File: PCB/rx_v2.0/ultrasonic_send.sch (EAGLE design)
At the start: 30 parts, among them J1 SBWD, J2 UART, J3 AD, J4 function, J5 pwr_5V, J6 AD, Q3 AMS1117-3.3

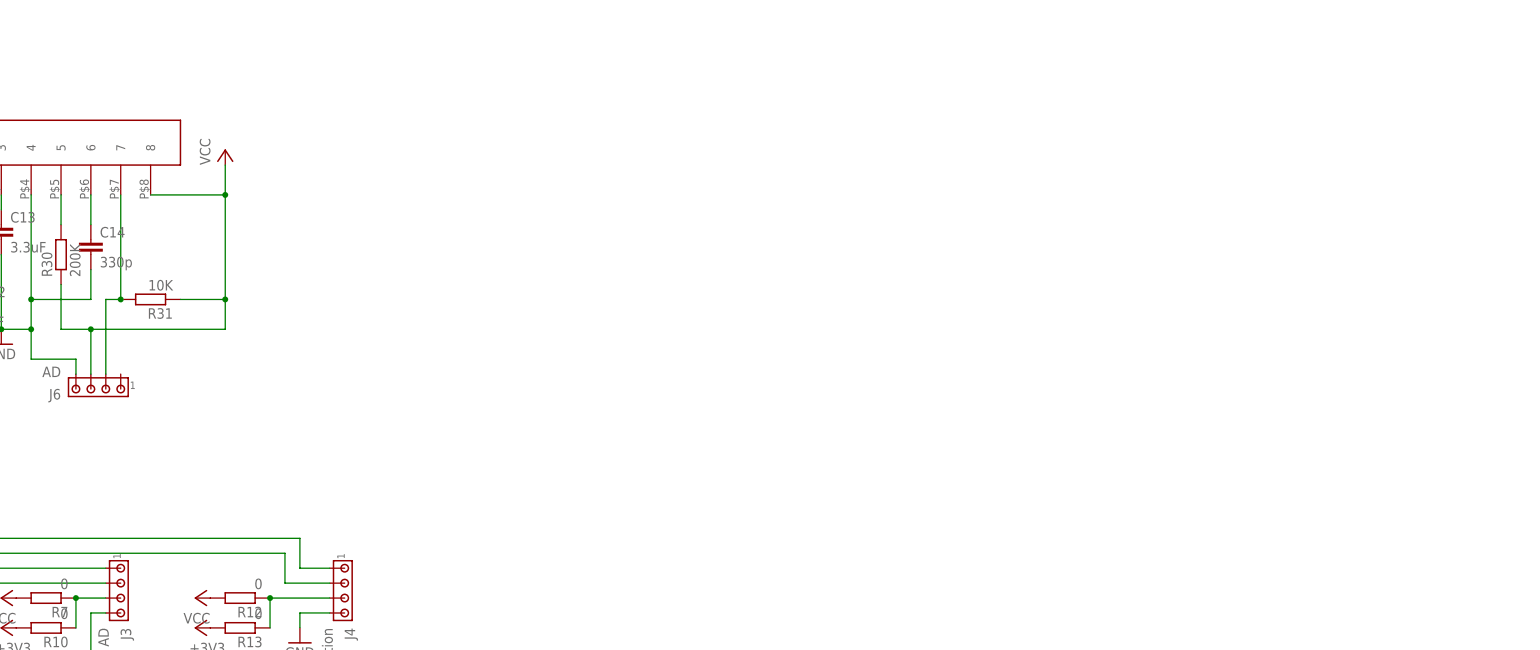
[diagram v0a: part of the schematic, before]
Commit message: 2.0 PCB finished with CC1101 and reveive modules.
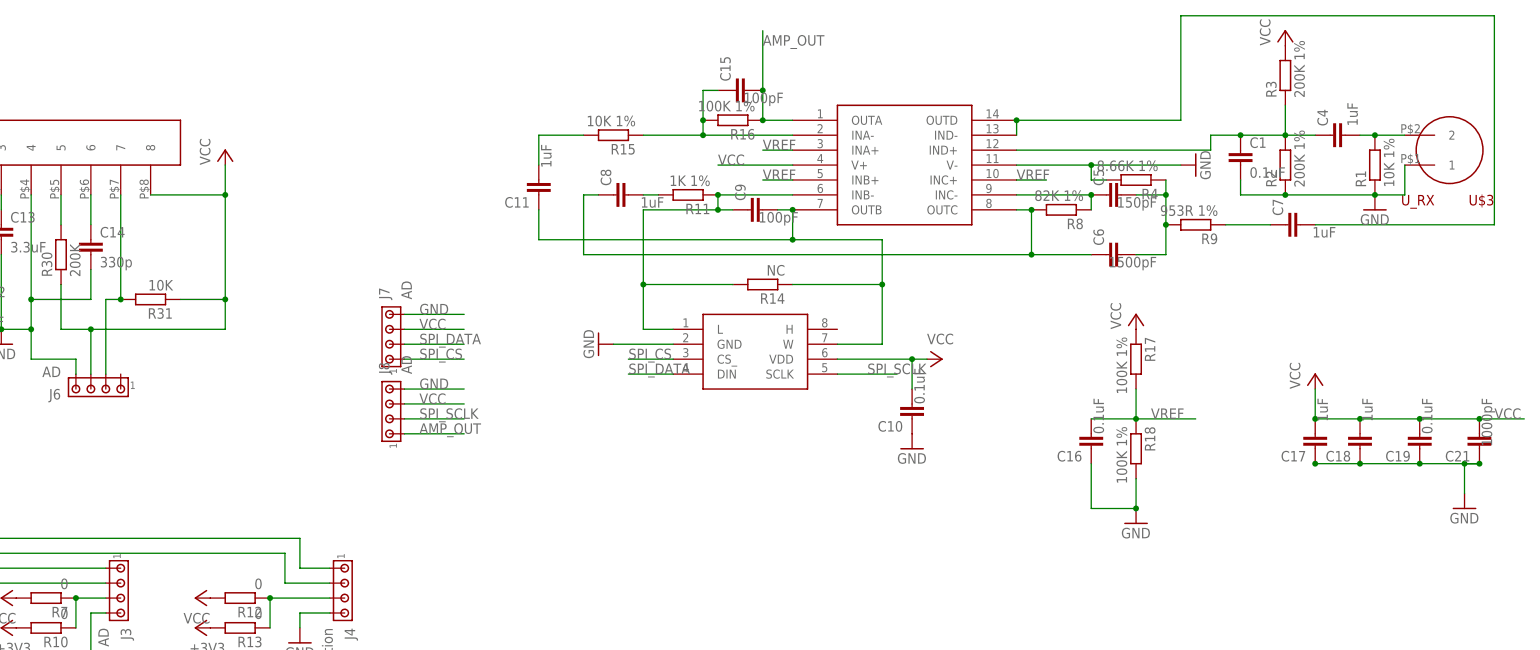
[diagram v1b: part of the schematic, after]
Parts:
- added C1, C10, C16, C19: 0.1uF, resistor:C-EUC0805
- added C11, C17, C18, C4, C7, C8: 1uF, resistor:C-EUC0805
- added C15, C9: 100pF, resistor:C-EUC0805
- added C21: 1000pF, resistor:C-EUC0805
- added C5: 150pF, resistor:C-EUC0805
- added C6: 1500pF, resistor:C-EUC0805
- added J7, J8: AD, con-amp:MTA04-100
- added R1, R15: 10K 1%, resistor:R-EU_R0603
- added R11: 1K 1%, resistor:R-EU_R0603
- added R14: NC, resistor:R-EU_R0603
- added R16, R17, R18: 100K 1%, resistor:R-EU_R0603
- added R2, R3: 200K 1%, resistor:R-EU_R0603
- added R4: 8.66K 1%, resistor:R-EU_R0603
- added R8: 82K 1%, resistor:R-EU_R0603
- added R9: 953R 1%, resistor:R-EU_R0603
- added U$1: OPA1654PW, tofu:OPA1654PW
- added U$3: U_RX, tofu:ULTRASONIC
- added U$5: MAX5401EKA-T, tofu:MAX5401EKA-T
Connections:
- new net AMP_OUT: C15.2, J8.1, R16.1, U$1.OUTA
- new net N$1: C4.2, R1.2, U$3.2
- new net N$2: C5.1, R8.1, U$1.INC-
- new net N$21: C7.1, R9.1
- new net N$22: C7.2, U$1.IND-, U$1.OUTD
- new net N$23: C9.1, R11.1, R14.2, U$1.INB-, U$5.L
- new net N$24: C11.1, C9.2, R14.1, U$1.OUTB, U$5.W
- new net N$25: C8.2, R11.2
- new net N$26: C11.2, R15.2
- new net N$27: C15.1, R15.1, R16.2, U$1.INA-
- new net N$3: C1.1, C4.1, R2.2, R3.1, U$1.IND+
- new net N$4: C6.1, C8.1, R8.2, U$1.OUTC
- new net N$8: C5.2, C6.2, R4.1, R9.2
- new net SPI_CS: J7.1, U$5.CS_
- new net SPI_DATA: J7.2, U$5.DIN
- new net SPI_SCLK: J8.2, U$5.SCLK
- new net VREF: C16.2, R17.2, R18.1, U$1.INA+, U$1.INB+, U$1.INC+
- net GND: now also C1.2, C10.1, C16.1, C17.1, C18.1, C19.1, C21.1, J7.4, J8.4, R1.1, R18.2, R2.1, R4.2, U$1.V-, U$3.1, U$5.GND
- net VCC: now also C10.2, C17.2, C18.2, C19.2, C21.2, J7.3, J8.3, R17.1, R3.2, U$1.V+, U$5.VDD
